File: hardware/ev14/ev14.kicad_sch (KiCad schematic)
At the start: 170 parts, among them CN1 Conn_05x02_Female, CN2 PJ-242, J1 USB_C_Receptacle, J10 Conn_02x04_Odd_Even, J11 Conn_02x05_Counter_Clockwise, J2 Conn_01x02_Socket, J3 AudioJack4, J5 Conn_02x03_Odd_Even, J6 Conn_01x35_Socket, J7 Conn_02x05_Counter_Clockwise, J8 Conn_02x05_Counter_Clockwise, J9 Conn_02x05_Counter_Clockwise, Q1 2N7002, Q2 Q_Dual_NMOS_S1G1D2S2G2D1, Q3 PMOS, SW1 SW_SPDT, SW2 SW_Push, SW3 SW_Push, SW4 SW_Push, SW5 SW_Push, U1 BQ21040DBV, U10 STM32F405RGTx, U2 USBLC6-2P6, U3 STM32F072CBTx, U4 CH340C, U5 TPS63060, U6 WM8960CGEFL/RV, U7 ESP32-S3-WROOM-1, U8 M24C02-RMN6TP, U9 BM14B(0.8)-24DS-0.4V(53), Y1 Crystal_GND24

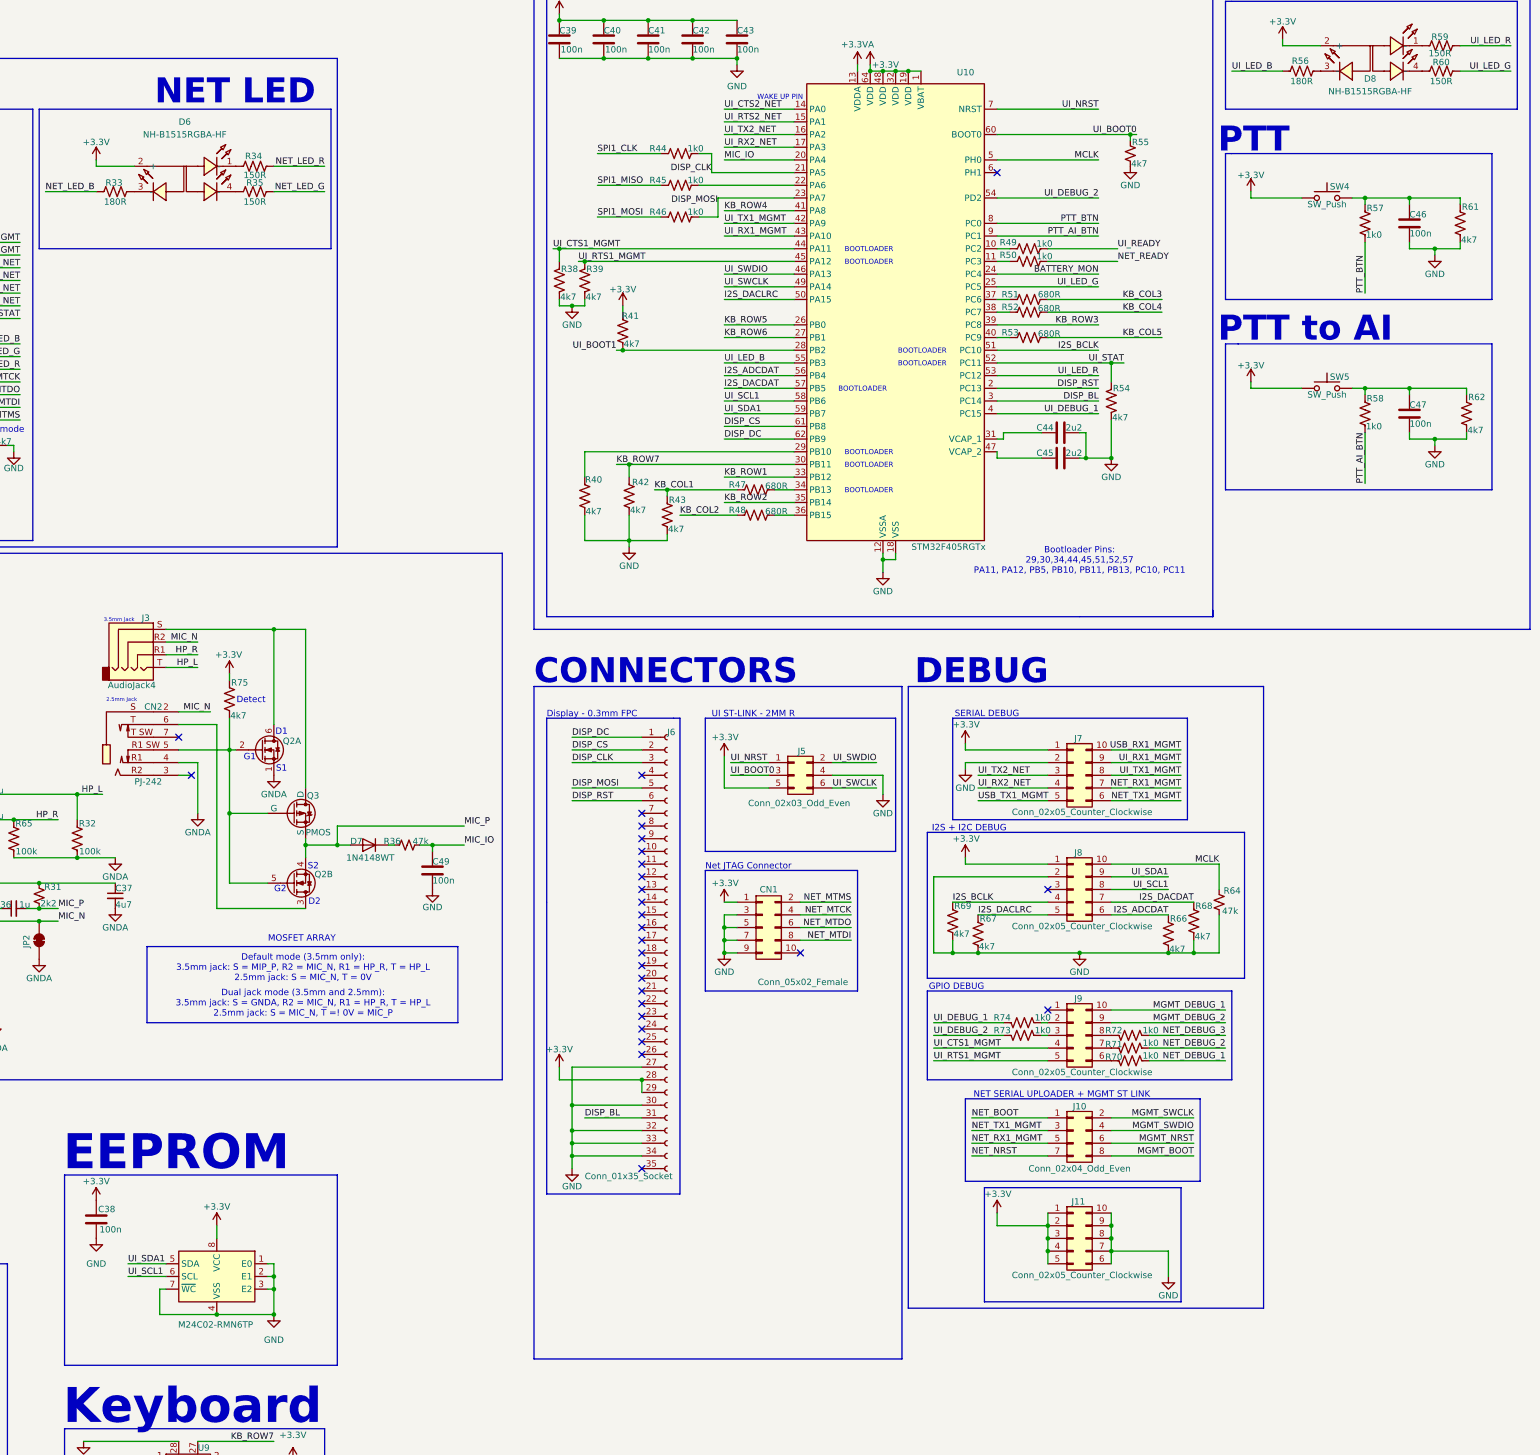
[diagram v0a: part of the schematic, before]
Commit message: feat: update to using kenwood k-plug and use a analog multiplexer to handle the changes in wiring. Add earpiece mega schematic
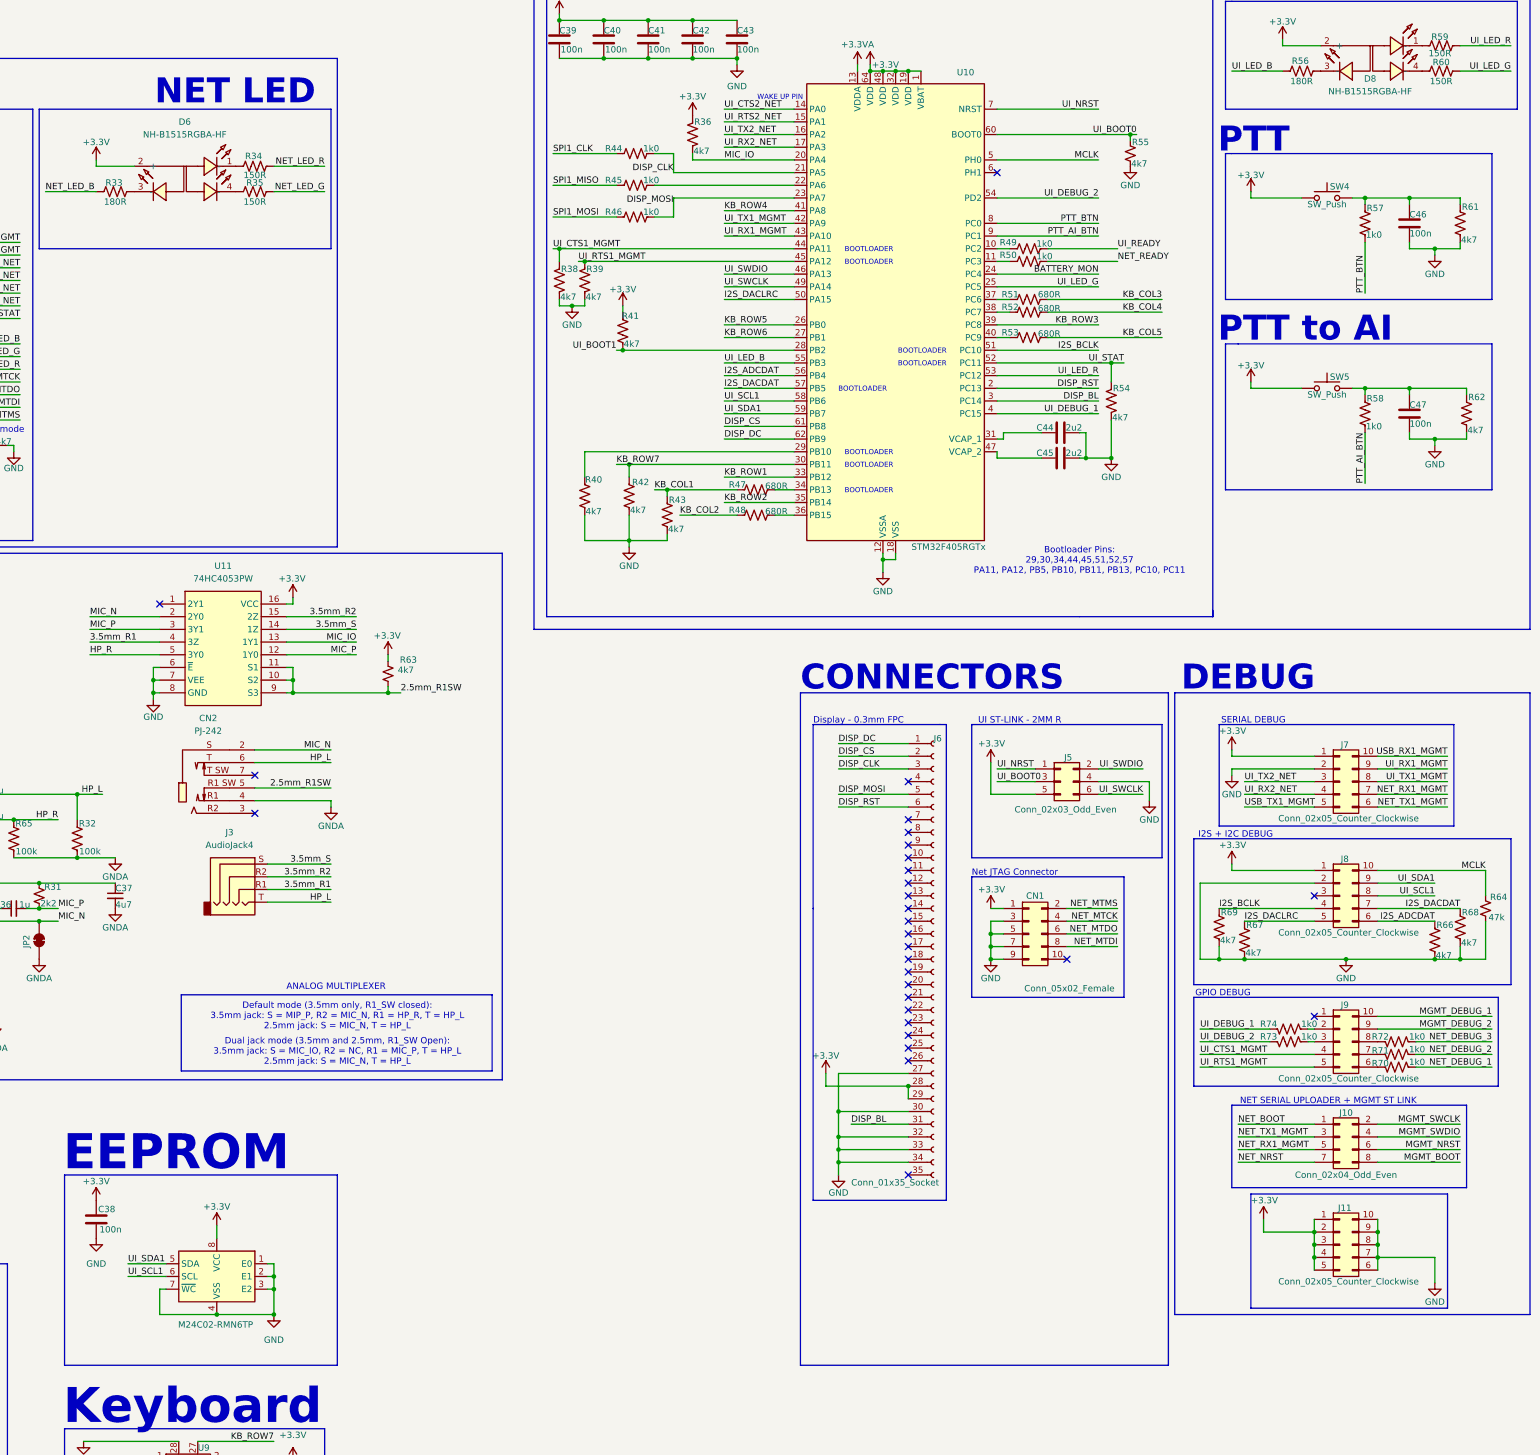
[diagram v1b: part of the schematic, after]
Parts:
- removed C49: 100n, Capacitor_SMD:C_0402_1005Metric, symbol Device:C
- removed CN2: PJ-242, Hactar_Footprints:AUDIO-SMD_PJ-242D-SMT, symbol Hactar_Symbols:PJ-242
- removed D7: 1N4148WT, Diode_SMD:D_SOD-523, symbol Device:D
- removed Q2: Q_Dual_NMOS_S1G1D2S2G2D1, Hactar_Footprints:SOT-363_L2.1-W1.3-P0.65-LS2.3-BL, symbol Transistor_FET:Q_Dual_NMOS_S1G1D2S2G2D1
- removed Q3: PMOS, Hactar_Footprints:SOT-23-3_L2.9-W1.3-P1.90-LS2.4-BR, symbol Simulation_SPICE:PMOS
- removed R36: 47k, Resistor_SMD:R_0402_1005Metric, symbol Device:R_Small_US
- removed R75: 4k7, Resistor_SMD:R_0402_1005Metric, symbol Device:R_US
- added CN2: PJ-242, hactar_footprints:AUDIO-SMD_PJ-242, symbol hactar_symbols:PJ-242
- added R36: 4k7, Resistor_SMD:R_0402_1005Metric, symbol Device:R_US
- added R63: 4k7, Resistor_SMD:R_0402_1005Metric, symbol Device:R_Small_US
- added U11: 74HC4053PW, 74HC4053:TSSOP-16_L5.0-W4.4-P0.65-LS6.4-BL, symbol Hactar_Symbols:74HC4053PW
- J3: footprint Hactar_Footprints:AUDIO-SMD_PJ-320D -> (none); JLCPCB Part # C431535 -> (none)
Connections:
- net +3.3V: now also R36.2, R63.2, U11.16 (VCC)
- net GND: now also U11.6 (~{E}), U11.7 (VEE), U11.8 (GND)
- net GNDA: now also CN2.4
- net HP_L: now also CN2.6
- net HP_R: now also U11.5 (3Y0); no longer J3.R1
- net MIC_IO: now also R36.1, U11.13 (1Y1)
- net MIC_N: now also CN2.2, U11.2 (2Y0); no longer J3.R2
- net MIC_P: now also U11.12 (1Y0), U11.3 (3Y1)
- net 3.5mm_S: now reaches J3.S
- net 3.5mm_S: now also U11.14 (1Z)
- new net 2.5mm_R1SW: CN2.5, R63.1, U11.10 (S2), U11.11 (S1), U11.9 (S3)
- new net 3.5mm_R1: J3.R1, U11.4 (3Z)
- new net 3.5mm_R2: J3.R2, U11.15 (2Z)
- no-connect marks 57 -> 58
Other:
- note added: "ANALOG MULTIPLEXER"
- note added: "Default mode (3.5mm only, R1_SW closed): 3.5mm jack: S = MIP_P, R2 = MIC_N, R1 = HP_R, T = HP_L 2.5mm jack: S = MIC_N, T = HP_L"
- note added: "Dual jack mode (3.5mm and 2.5mm, R1_SW Open): 3.5mm jack: S = MIC_IO, R2 = NC, R1 = MIC_P, T = HP_L 2.5mm jack: S = MIC_N, T = HP_L"
- note removed: "2.5mm Jack"
- note removed: "3.5mm Jack"
- note removed: "D1"
- note removed: "D2"
- note removed: "Default mode (3.5mm only): 3.5mm jack: S = MIP_P, R2 = MIC_N, R1 = HP_R, T = HP_L 2.5mm jack: S = MIC_N, T = 0V"
- note removed: "Detect"
- note removed: "Dual jack mode (3.5mm and 2.5mm): 3.5mm jack: S = GNDA, R2 = MIC_N, R1 = HP_R, T = HP_L 2.5mm jack: S = MIC_N, T =! 0V = MIC_P"
- note removed: "G1"
- note removed: "G2"
- note removed: "MOSFET ARRAY"
- note removed: "S1"
- note removed: "S2"
- moved on the sheet: CN1, J10, J11, J5, J6, J7, J8, J9, R44, R45, R46, R64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

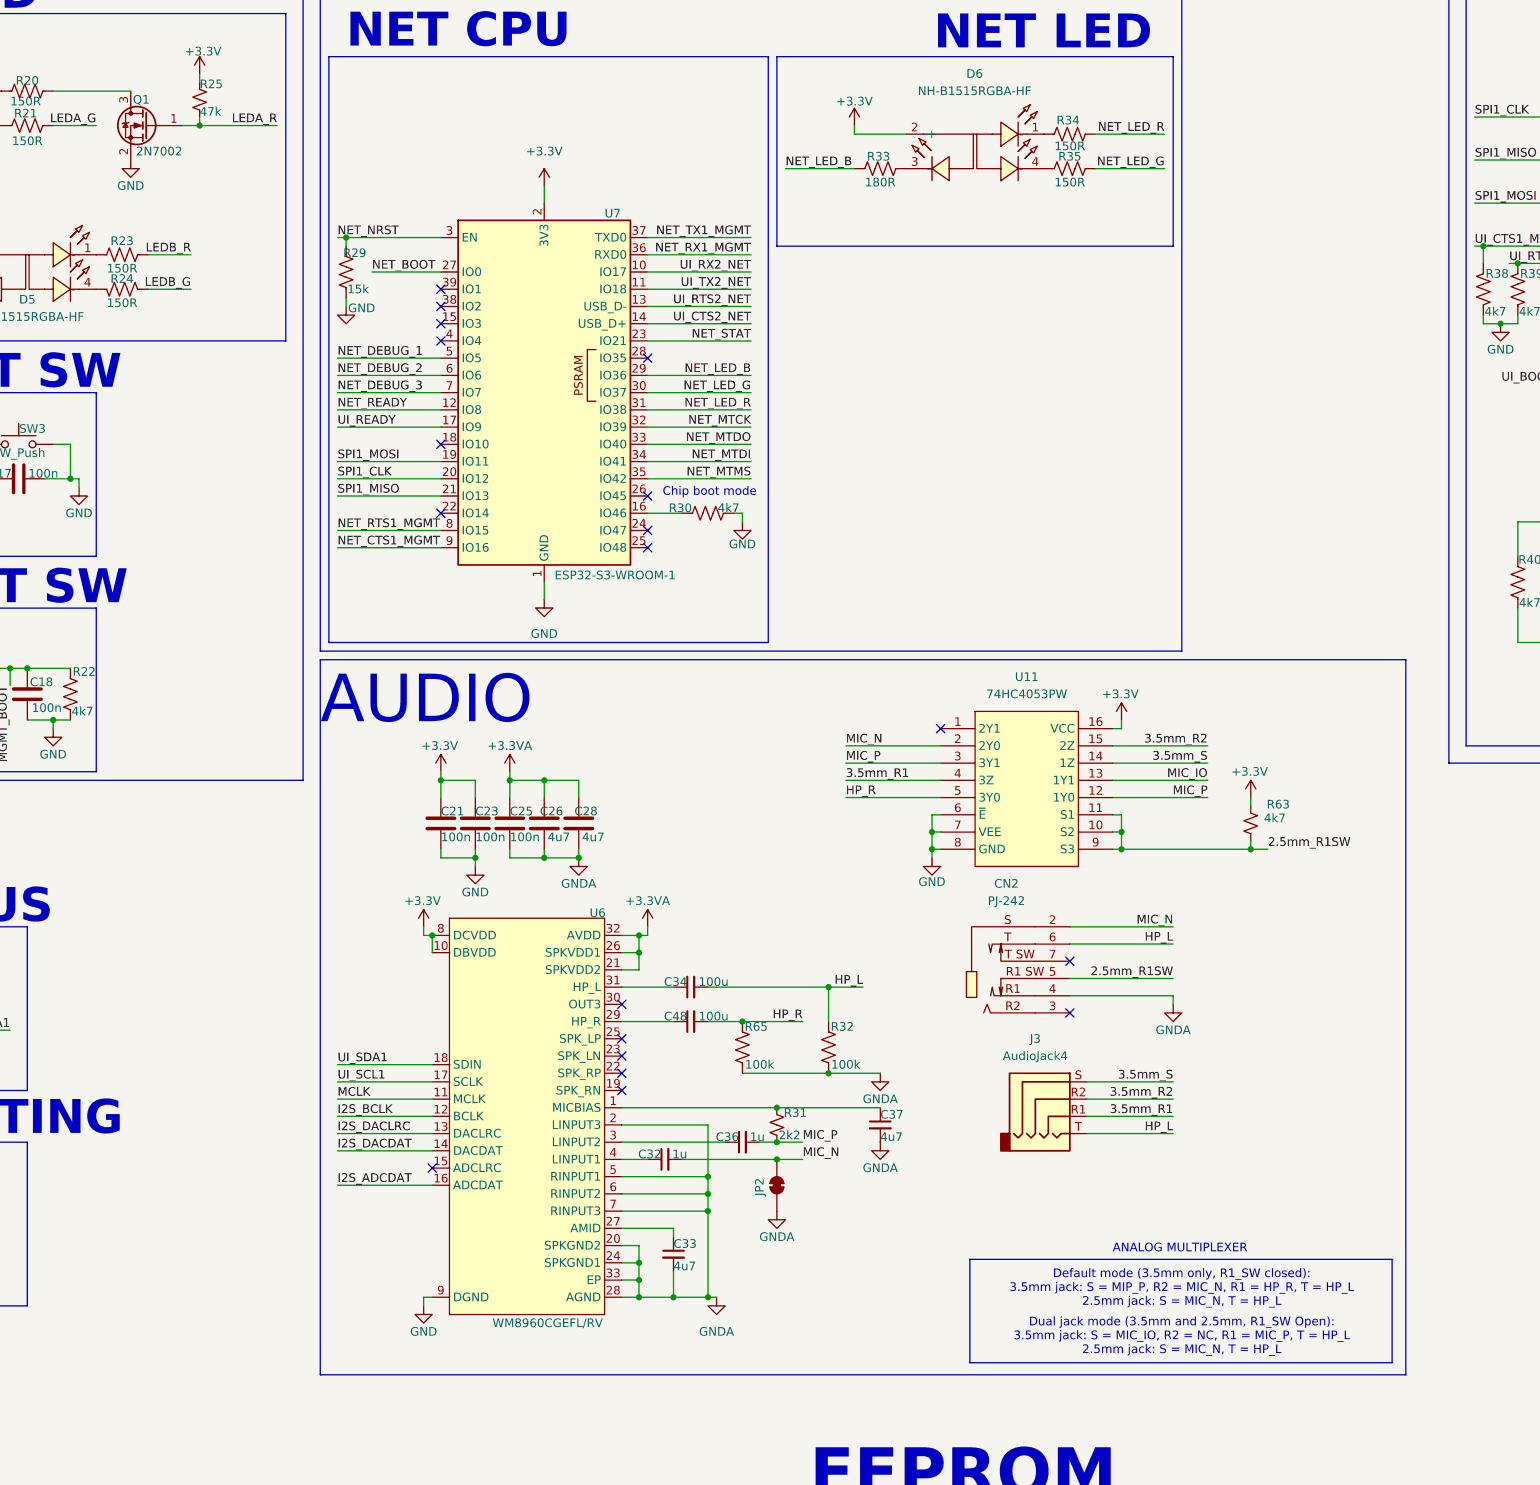
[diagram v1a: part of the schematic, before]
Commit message: chore: update headphone jacks to be 11.46mm apart. Fix issues that arose from that
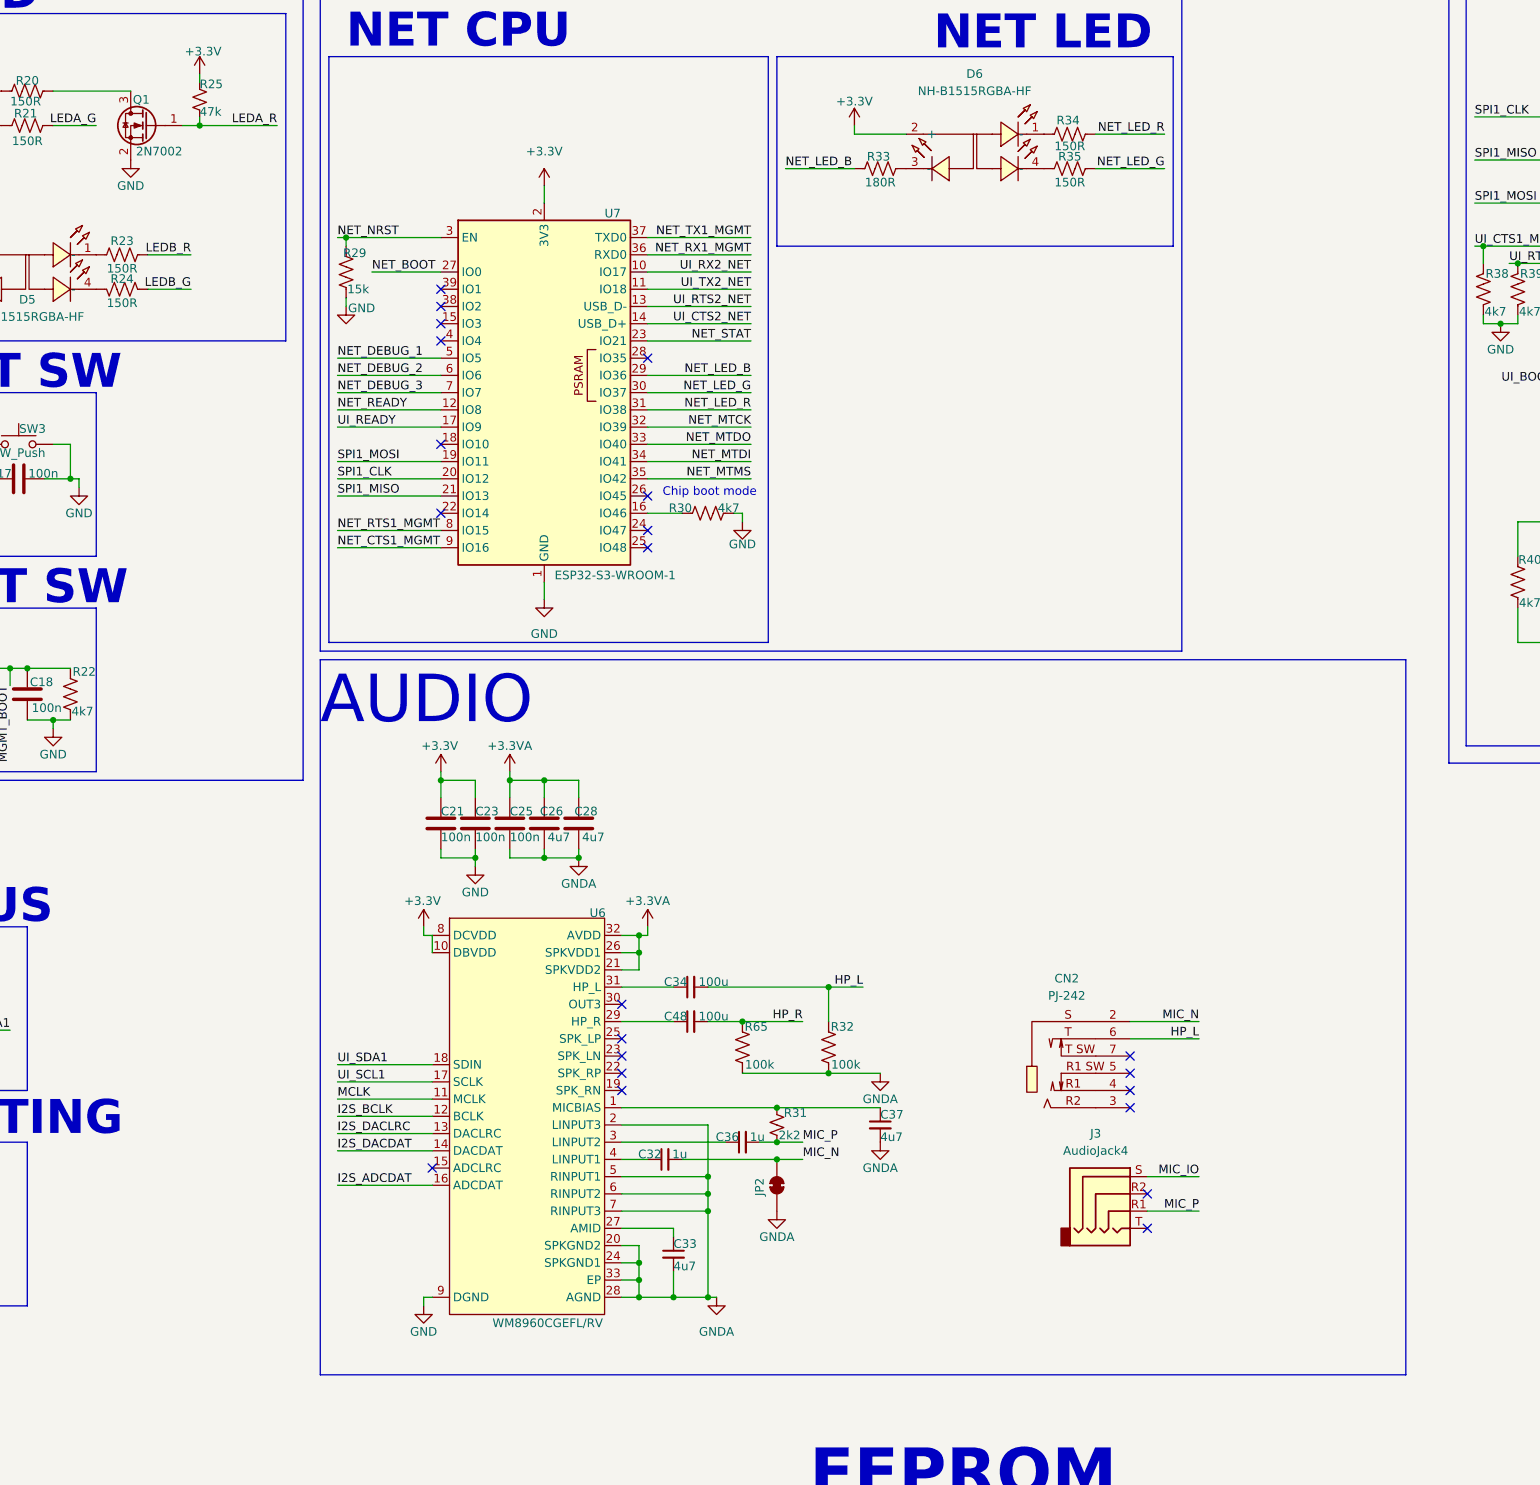
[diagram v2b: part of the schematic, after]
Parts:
- removed R63: 4k7, Resistor_SMD:R_0402_1005Metric, symbol Device:R_Small_US
- removed U11: 74HC4053PW, 74HC4053:TSSOP-16_L5.0-W4.4-P0.65-LS6.4-BL, symbol Hactar_Symbols:74HC4053PW
- CN2: footprint hactar_footprints:AUDIO-SMD_PJ-242 -> Hactar_Footprints:AUDIO-SMD_PJ-242D-SMT; symbol hactar_symbols:PJ-242 -> Hactar_Symbols:PJ-242
- J3: footprint (none) -> Hactar_Footprints:AUDIO-SMD_PJ-320D
- U6: symbol Hactar_Symbols:WM8960CGEFL/RV_1 -> Hactar_Symbols:WM8960CGEFL/RV
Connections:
- net 3.5mm_R1 is gone; now on net MIC_P: J3.R1
- net 3.5mm_S is gone; now on net MIC_IO: J3.S
- net GNDA: no longer CN2.4
- net HP_L: no longer J3.T
- net 2.5mm_R1SW: no longer names the net of CN2.5
- net 3.5mm_R2: no longer names the net of J3.R2
- no-connect marks 58 -> 61
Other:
- note removed: "ANALOG MULTIPLEXER"
- note removed: "Default mode (3.5mm only, R1_SW closed): 3.5mm jack: S = MIP_P, R2 = MIC_N, R1 = HP_R, T = HP_L 2.5mm jack: S = MIC_N, T = HP_L"
- note removed: "Dual jack mode (3.5mm and 2.5mm, R1_SW Open): 3.5mm jack: S = MIC_IO, R2 = NC, R1 = MIC_P, T = HP_L 2.5mm jack: S = MIC_N, T = HP_L"
- moved on the sheet: CN2, J3
